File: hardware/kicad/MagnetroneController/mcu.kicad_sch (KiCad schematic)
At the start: 1 part, among them U10 Teensy4.1

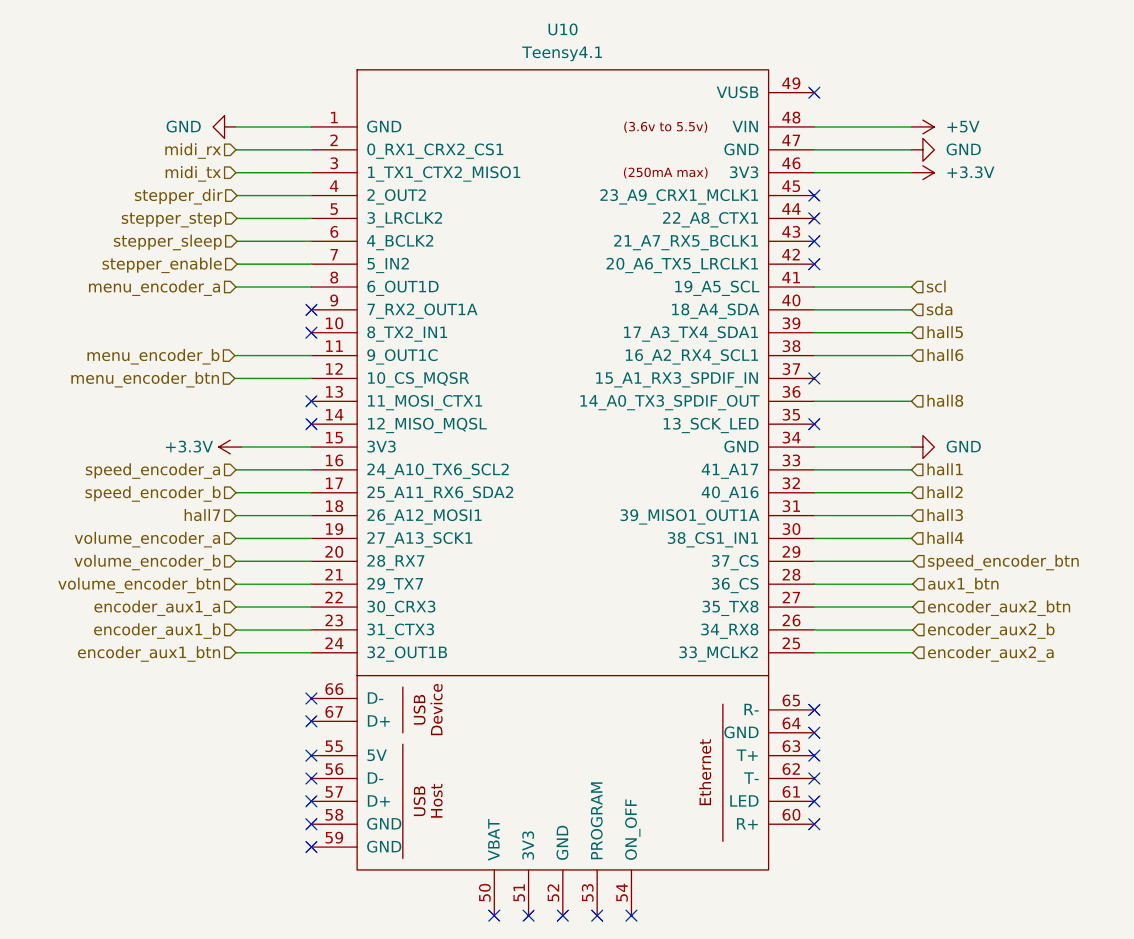
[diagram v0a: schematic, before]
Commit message: chore: replace motor driver
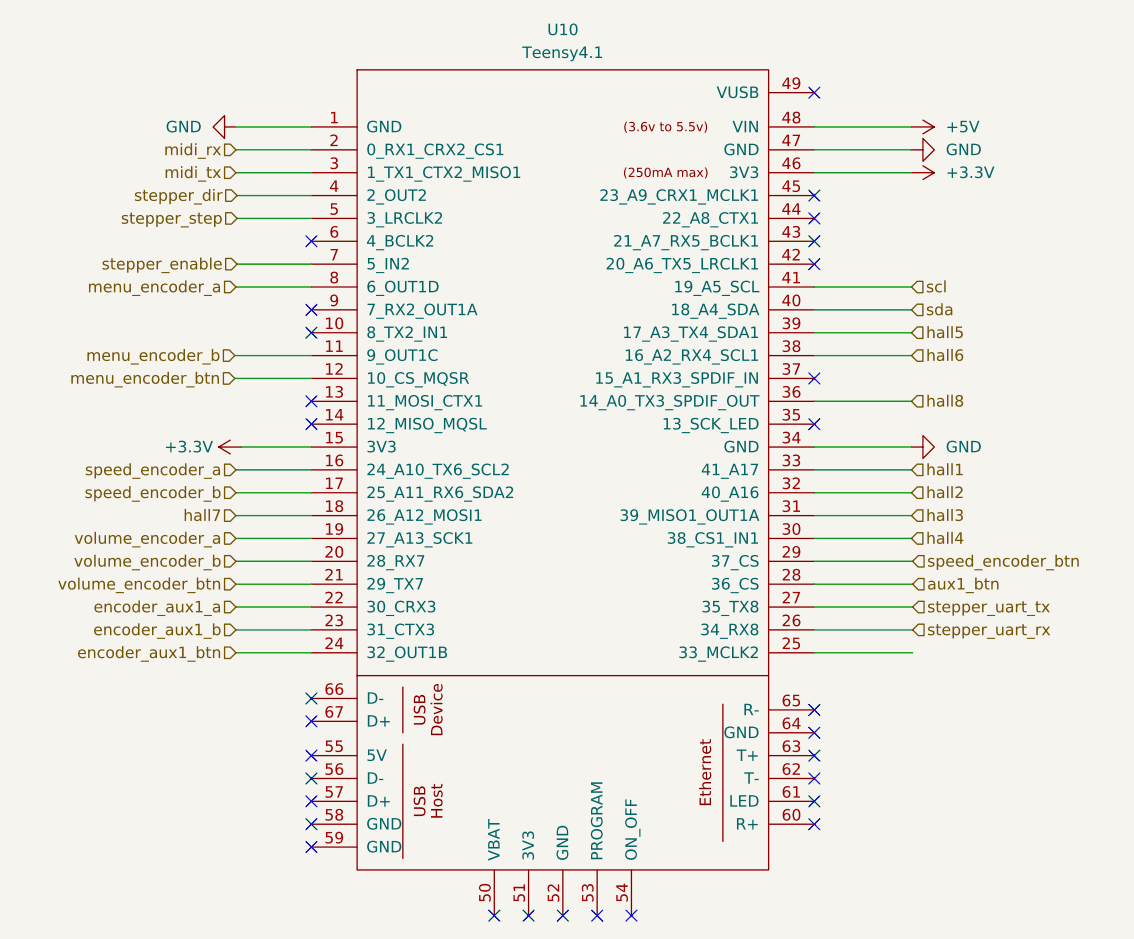
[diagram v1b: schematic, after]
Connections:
- net encoder_aux2_a: no longer names the net of U10.25 (33_MCLK2)
- net encoder_aux2_b renamed stepper_uart_rx
- net encoder_aux2_btn renamed stepper_uart_tx
- net stepper_sleep: no longer names the net of U10.6 (4_BCLK2)
- no-connect marks 29 -> 30
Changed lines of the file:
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@@
+	)
+	(no_connect
+		(at 100.33 60.96)
 	)
 	(no_connect
@@
 	(wire
 		(pts
-			(xy 92.075 60.96) (xy 100.33 60.96)
-		)
-		(stroke
-			(width 0)
-			(type default)
-		)
-	)
-	(wire
-		(pts
 			(xy 91.948 53.34) (xy 100.33 53.34)
 		)
@@
 		)
 	)
+	(hierarchical_label "stepper_uart_rx"
+		(shape input)
+		(at 167.132 104.14 0)
+		(effects
+			(font
+				(size 1.27 1.27)
+			)
+			(justify left)
+		)
+	)
+	(hierarchical_label "stepper_uart_tx"
+		(shape input)
+		(at 167.132 101.6 0)
+		(effects
+			(font
+				(size 1.27 1.27)
+			)
+			(justify left)
+		)
+	)
 	(hierarchical_label "menu_encoder_btn"
 		(shape input)
@@
 		)
 	)
-	(hierarchical_label "encoder_aux2_a"
-		(shape input)
-		(at 167.132 106.68 0)
-		(effects
-			(font
-				(size 1.27 1.27)
-			)
-			(justify left)
-		)
-	)
 	(hierarchical_label "volume_encoder_btn"
 		(shape input)
@@
 		)
 	)
-	(hierarchical_label "stepper_sleep"
-		(shape input)
-		(at 92.075 60.96 180)
-		(effects
-			(font
-				(size 1.27 1.27)
-			)
-			(justify right)
-		)
-	)
 	(hierarchical_label "volume_encoder_a"
 		(shape input)
@@
 		)
 	)
-	(hierarchical_label "encoder_aux2_btn"
-		(shape input)
-		(at 167.132 101.6 0)
-		(effects
-			(font
-				(size 1.27 1.27)
-			)
-			(justify left)
-		)
-	)
 	(hierarchical_label "scl"
 		(shape input)
@@
 		)
 	)
-	(hierarchical_label "encoder_aux2_b"
-		(shape input)
-		(at 167.132 104.14 0)
-		(effects
-			(font
-				(size 1.27 1.27)
-			)
-			(justify left)
-		)
-	)

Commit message: feat: cleanup
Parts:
- U10: footprint teensy:Teensy41 -> magnetrone:Teensy41_AudioShield_RevD
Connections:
- net hall1: now also U10.39 (17_A3_TX4_SDA1); no longer U10.33 (41_A17)
- net hall2: now also U10.36 (14_A0_TX3_SPDIF_OUT); no longer U10.32 (40_A16)
- net hall5: now also U10.32 (40_A16); no longer U10.39 (17_A3_TX4_SDA1)
- net hall6: now also U10.33 (41_A17); no longer U10.38 (16_A2_RX4_SCL1)
- net hall7: now also U10.38 (16_A2_RX4_SCL1); no longer U10.18 (26_A12_MOSI1)
- net hall8: now also U10.18 (26_A12_MOSI1); no longer U10.36 (14_A0_TX3_SPDIF_OUT)
- net volume_encoder_a: now also U10.21 (29_TX7); no longer U10.19 (27_A13_SCK1)
- net volume_encoder_b: now also U10.19 (27_A13_SCK1); no longer U10.20 (28_RX7)
- net volume_encoder_btn: now also U10.20 (28_RX7); no longer U10.21 (29_TX7)
- no-connect marks 30 -> 31
